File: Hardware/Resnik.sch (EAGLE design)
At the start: 99 parts, among them J2 CONN_82.54_SCREW, J3 CONN_42.54_SCREW, J4 CONN_82.54_SCREW, Q1 DMG3404, Q2 DMG3404, Q3 FDN360P, Q4 FDN360P, U1 TPS61030RSA, U10 MIC2039MT, U11 MIC2039MT, U12 SN74AUP2G08DQE, U13 SN74AUP1G04DCK, U14 MIC2039MT, U15 MIC2039MT, U16 SN74AUP2G08DQE, U17 SN74AUP1G04DCK, U18 TXS0102DQM, U19 LTC4412S6, U2 TPS62822DLC, U3 TLV61220DBV, U4 BQ2980RUG, U6 TPS22917DBV, U7 TPS22917DBV, U8 SN74AUP2G08DQE, U9 SN74AUP2G86SOT833-1

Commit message: Continued schematic additions, prelim part placement
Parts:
- removed R6: 180k, bschulz_passives:R-EU_R0603
- removed R7: 820k, bschulz_passives:R-EU_R0603
- removed U$18: TPS2105, bschulz:TPS2105
- removed U$6: TPS79733, bschulz:TPS79733
- added C22, C24, C28: 0.1uF, bschulz_passives:C-EU0.1UFC0402
- added C23: 10uF, bschulz_passives:C-EU10UFC0805
- added C25: 1uF, bschulz_passives:C-EU0.1UFC0402
- added C26, C27, CX2, CX3: 12pF, bschulz_passives:C-EU12PFC0402
- added C29, C31, C32, C33, C34, C35, C36: 0.1uF, bschulz_passives:C-EUC0402
- added C30: 10uF, bschulz_passives:C-EUC0805
- added D+, D-: 27, bschulz_passives:R-EU_27R0402
- added D2, D3: (no value), bschulz:LM40402.5
- added D4, D5: (no value), bschulz:DIODEDO-214AC
- added F1: PPTC1.5A, bschulz:PPTC1.5A
- added IC1: ATMEGA644M, bschulz:ATMEGA644M
- added ISP2: AVRISP-6, bschulz:AVRISP-6
- added J5, J6, J7: (no value), bschulz:CONN_02SCREW_2.54
- added J8: (no value), bschulz:JST_2MM_MALE
- added JP5, JP6, JP7: JUMPER-SMT_2_NO_SILK, SparkFun-Jumpers:JUMPER-SMT_2_NO_SILK
- added MICRO_USB: MICRO_USB_LONGPADS, bschulz:MICRO_USB_LONGPADS
- added Q5: FDN360P, transistor-power:FDN360P
- added Q6: DMG3404, bschulz:MOSFET-NCH-DMG3404L
- added R35, R36, R37, R38, R39, R40, R41, R42: 330, bschulz_passives:R-EU_330R0402
- added R43, R44: 10k, bschulz_passives:R-EU_10KR0402
- added R45, R48, R49: 10k, bschulz_passives:R-EU_R0402
- added R46: 180k, bschulz_passives:R-EU_R0402
- added R47: 120k, bschulz:R-EU_R0603
- added R50: 330R, bschulz:R-EU_R0603
- added R51: (no value), bschulz:R-EU_R0603
- added R52, R53: 10k, bschulz_passives:R-EU_P10KR0603
- added U$1: CRYSTAL8MHZ5X3.2, bschulz:CRYSTAL8MHZ5X3.2
- added U$13: SN74LVC1G3157DRL, bschulz:SN74LVC1G3157DRL
- added U$15, U$16: CLVBA-FKA, bschulz:CLVBA-FKA
- added U$17: SN74AUP3G34DCU, bschulz:SN74AUP3G34DCU
- added U$2: MICROSD, bschulz:MICROSD
- added U$3: TPL5111DDC, bschulz:TPL5111DDC
- added U$5, U$9: BUTTON4.2X3.2, bschulz:BUTTON4.2X3.2
- added U20, U24: TPS22917DBV, bschulz:TPS22917DBV
- added U21: TXS0102DQM, bschulz:TXS0102DQM
- added U23: FT231X-Q, bschulz:FT231X-Q
- added U25, U26: TXS0108RGY, bschulz:TXS0108RGY
- added U27: TXS0104RGY, bschulz:TXS0104RGY
- added U28: MCP4726A2SOT-23, bschulz:MCP4726A2SOT-23
- added U29, U30: ADS1115, bschulz:ADS1115
- added U31: INA211DCK, bschulz:INA211DCK
- added U32: INA210DCK, bschulz:INA210DCK
- added U33: TCA9555RTW, bschulz:TCA9555RTW
- C1: value 22uF -> 4.7uF
- C10: value 0.1uF -> 22uF; device bschulz_passives:C-EUC0402 -> bschulz_passives:C-EUC0805
- C12: value 22uF -> 0.1uF; device bschulz_passives:C-EUC0805 -> bschulz_passives:C-EUC0402
- C13: value 10uF -> 1uF; device bschulz_passives:C-EUC0805 -> bschulz_passives:C-EUC0603
- C14: value 1uF -> 10uF; device bschulz_passives:C-EUC0603 -> bschulz_passives:C-EUC0805
- C15, C16: value 22uF -> 0.1uF; device bschulz_passives:C-EUC0805 -> bschulz_passives:C-EU0.1UFC0402
- C18: value 0.1uF -> 1uF; device bschulz_passives:C-EU0.1UFC0402 -> bschulz_passives:C-EU1UFC0603
- C19, C20: value 0.1uF -> 22uF; device bschulz_passives:C-EU0.1UFC0402 -> bschulz_passives:C-EUC0805
- C2: value 220uF -> 22uF; device bschulz_passives:CTANT_EU2917 -> bschulz_passives:C-EUC0805
- C21: value 1uF -> 0.1uF; device bschulz_passives:C-EU1UFC0603 -> bschulz_passives:C-EU0.1UFC0402
- C3: value 2.2uF -> 10uF
- C4: value 4.7uF -> 10uF
- C5: value 68pF -> 220uF; device bschulz_passives:C-EUC0402 -> bschulz_passives:CTANT_EU2917
- C6: value 22uF -> 68pF; device bschulz_passives:C-EUC0805 -> bschulz_passives:C-EUC0402
- C7: value 22uF -> 2.2uF
- C8, C9: value 10uF -> 22uF
- J1: value (none) -> CONN_82.54_SCREW; device bschulz:CONN_102.54_SCREW -> bschulz:CONN_82.54_SCREW
- J2: value CONN_82.54_SCREW -> (none); device bschulz:CONN_82.54_SCREW -> bschulz:CONN_102.54_SCREW
- J3: value CONN_42.54_SCREW -> CONN_82.54_SCREW; device bschulz:CONN_42.54_SCREW -> bschulz:CONN_82.54_SCREW
- J4: value CONN_82.54_SCREW -> CONN_42.54_SCREW; device bschulz:CONN_82.54_SCREW -> bschulz:CONN_42.54_SCREW
- L1: value 10uH -> 6.8uH; device bschulz:INDUCTORXHMI_6.65X6.45 -> bschulz:INDUCTOR1008
- L2: value 1uH -> 10uH; device bschulz:INDUCTORLQS_3X3 -> bschulz:INDUCTORXHMI_6.65X6.45
- L3: value 6.8uH -> 1uH; device bschulz:INDUCTOR1008 -> bschulz:INDUCTORLQS_3X3
- R1, R9: value 1.62M -> 180k
- R11: value 20R -> 330R
- R12: value 330R -> 3m; device bschulz:R-EU_R0402 -> bschulz_passives:R-EU_R0805
- R13: value (none) -> 20R
- R14: value 100R -> (none)
- R15: value 2k -> 91k
- R16: value 3m -> 100R; device bschulz_passives:R-EU_R0805 -> bschulz:R-EU_R0402
- R17: value 91k -> 2k
- R2: value 360k -> 1.62M
- R21: value 10k -> (none); device bschulz_passives:R-EU_R0402 -> bschulz:R-EU_R0603
- R22: value 287R -> 10k; device bschulz_passives:R-EU_R0603 -> bschulz_passives:R-EU_10KR0402
- R23, R24, R25: value 287R -> 10k; device bschulz_passives:R-EU_R0603 -> bschulz_passives:R-EU_R0402
- R27, R28, R29, R30: device bschulz_passives:R-EU_R0603 -> bschulz_passives:R-EU_R0402
- R3: value 1.62M -> 360k
- R31, R32: value 10k -> 287R
- R33: value 10k -> 287R; device bschulz_passives:R-EU_10KR0402 -> bschulz_passives:R-EU_R0402
- R34: value (none) -> 287R; device bschulz:R-EU_R0603 -> bschulz_passives:R-EU_R0402
- R4: value 180k -> 1.62M
- R8: value 180k -> 820k
- U1: value TPS61030RSA -> TLV61220DBV; device bschulz:TPS61030RSA -> bschulz:TLV61220DBV
- U10: value MIC2039MT -> SN74AUP1G04DCK; device bschulz:MIC2039MT -> bschulz:SN74AUP1G04DCK
- U11: value MIC2039MT -> SN74AUP2G86SOT833-1; device bschulz:MIC2039MT -> bschulz:SN74AUP2G86SOT833-1
- U13: value SN74AUP1G04DCK -> SN74AUP2G08DQE; device bschulz:SN74AUP1G04DCK -> bschulz:SN74AUP2G08DQE
- U14: value MIC2039MT -> SN74AUP2G08DQE; device bschulz:MIC2039MT -> bschulz:SN74AUP2G08DQE
- U16: value SN74AUP2G08DQE -> MIC2039MT; device bschulz:SN74AUP2G08DQE -> bschulz:MIC2039MT
- U17: value SN74AUP1G04DCK -> MIC2039MT; device bschulz:SN74AUP1G04DCK -> bschulz:MIC2039MT
- U18: value TXS0102DQM -> MIC2039MT; device bschulz:TXS0102DQM -> bschulz:MIC2039MT
- U19: value LTC4412S6 -> TPS22917DBV; device bschulz:LTC4412S6 -> bschulz:TPS22917DBV
- U3: value TLV61220DBV -> TPS61032RSA; device bschulz:TLV61220DBV -> bschulz:TPS61032RSA
- U4: value BQ2980RUG -> (none); device bschulz:BQ2980RUG -> bschulz:LT3652DD
- U5: value (none) -> BQ2980RUG; device bschulz:LT3652DD -> bschulz:BQ2980RUG
- U6: value TPS22917DBV -> TPS2105; device bschulz:TPS22917DBV -> bschulz:TPS2105
- U7: value TPS22917DBV -> LTC4412S6; device bschulz:TPS22917DBV -> bschulz:LTC4412S6
- U8: value SN74AUP2G08DQE -> TPS79733; device bschulz:SN74AUP2G08DQE -> bschulz:TPS79733
- U9: value SN74AUP2G86SOT833-1 -> SN74AUP1G04DCK; device bschulz:SN74AUP2G86SOT833-1 -> bschulz:SN74AUP1G04DCK
- renumbered U$12 to U22
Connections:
- removed net N$1: R3.1, R4.2, U1.FB
- removed net N$17: U6.QOD, U6.VOUT
- removed net N$19: U7.QOD, U7.VOUT
- removed net N$42: R32.2, S2.P
- removed net N$9 (its old number): L3.2, U3.SW
- new net 3V3: C25.1, IC1.AREF, IC1.AVCC, IC1.VCC, IC1.VCC@1, IC1.VCC@2, ISP2.VCC, R44.2, U$16.ANODE
- new net 3V3_AUX_CTRL: IC1.(PCINT22/TOSC1)PC6
- new net 3V3_FTDI: C24.1, U23.3V3OUT, U23.RESET#, U23.VCCIO
- new net ADC_0: JP7.1, U30.AIN0
- new net ADC_1: U30.AIN1
- new net ADC_2: U30.AIN2
- new net ADC_3: JP6.1, U30.AIN3
- new net ADC_EXT: IC1.(PCINT0/ADC0)PA0
- new net ADC_EXT_ALERT: U30.ALERT
- new net ADC_OB_ALERT: U29.ALERT
- new net ALIVE_LED: IC1.(PCINT20/TDO)PC4, R39.2
- new net BAT_SENSE: IC1.(PCINT2/ADC2)PA2
- new net BUS_LOGIC_EN_PRIME: R48.1, U25.EN, U27.EN
- new net BUS_LOGIC_EN_SEC: R49.1, U26.EN
- new net CS_EXT: U27.A4
- new net CS_OUT: U27.B4
- new net DAC_OUT: C31.1, U28.VOUT
- new net DTR: C28.1, U23.DTR#
- new net EN_BUS_SEC: R25.1, U12.A1, U12.B2
- new net FEATHER_BAT: U24.QOD, U24.VOUT
- new net FEATHER_EN: Q5.G, R46.1
- new net GPIO_0: U25.A3
- new net GPIO_0_OUT: U25.B3
- new net GPIO_1: U25.A4
- new net GPIO_1_OUT: U25.B4
- new net GPIO_2: U26.A3
- new net GPIO_2_OUT: U26.B3
- new net GPIO_3: U26.A4
- new net GPIO_3_OUT: U26.B4
- new net GPIO_EXT: IC1.(PCINT11/OC0A/AIN1)PB3
- new net I_LI: U29.AIN2, U31.OUT
- new net I_SOLAR: U29.AIN0, U32.OUT
- new net LED1: IC1.(PCINT29/OC1A)PD5, R42.1
- new net LED2: IC1.(PCINT30/OC2B/ICP)PD6, R40.1
- new net LED3: IC1.(PCINT31/OC2A)PD7, R41.1
- new net LOG_INT: IC1.(PCINT4/ADC4)PA4, R43.1, U$5.3, U$5.4
- new net MISO: IC1.(PCINT14/MISO)PB6, ISP2.MISO, U$2.DATA_OUT, U27.A1
- new net MISO_OUT: U27.B1
- new net MOSI: IC1.(PCINT13/MOSI)PB5, ISP2.MOSI, U$17.2A, U27.A2
- new net MOSI_BUF: U$17.2Y, U$2.DATA_IN
- new net MOSI_OUT: U27.B2
- new net N$44: R38.2, U23.TXD
- new net N$47: R37.2, U23.RXD
- new net N$48: CX3.2, D+.2, MICRO_USB.D+
- new net N$49: CX2.2, D-.2, MICRO_USB.D-
- new net N$5: L2.2, U3.SW
- new net N$50: D+.1, U23.USBDP
- new net N$51: R36.2, U23.CBUS1
- new net N$52: D-.1, U23.USBDM
- new net N$53: R36.1, U$16.RED_CATH
- new net N$54: R35.1, U$16.BLUE_CATH
- new net N$56: R39.1, U$16.GREEN_CATH
- new net N$57: R35.2, U23.CBUS2
- new net N$58: R40.2, U$15.BLUE_CATH
- new net N$59: R41.2, U$15.GREEN_CATH
- new net N$60: R42.2, U$15.RED_CATH
- new net N$61: C27.2, IC1.XTAL2, U$1.2
- new net N$62: C26.2, IC1.XTAL1, U$1.1
- new net N$63: Q5.D, R47.2, U$3.DELAY
- new net N$64: U$3.DRVN, U24.ON
- new net N$65: JP7.2, R53.2
- new net N$66: JP6.2, R52.2
- new net N$67: C10.1, D5.C, U4.VIN, U4.VIN_REG
- new net PG: IC1.(PCINT18/TCK)PC2
- new net RST: C28.2, IC1.RESET, ISP2.RST, R44.1, U$9.3, U$9.4
- new net RX: IC1.(PCINT24/RXD0)PD0, R38.1
- new net RX_EXT: IC1.(PCINT26/INT0)PD2, U25.A6, U26.A6
- new net RX_OUT_PRIME: U25.B6
- new net RX_OUT_SEC: U26.B6
- new net SCK: IC1.(PCINT15/SCK)PB7, ISP2.SCK, U$17.1A, U27.A3
- new net SCK_BUF: U$17.1Y, U$2.SCLK
- new net SCK_OUT: U27.B3
- new net SCL_OUT_PRIME: U25.B2
- new net SCL_OUT_SEC: U26.B2
- new net SDA_CTRL: IC1.(PCINT21/TDI)PC5, U$13.S
- new net SDA_EXT: JP5.2, U$13.B2, U25.A1, U26.A1
- new net SDA_OUT_PRIME: U25.B1
- new net SDA_OUT_SEC: U26.B1
- new net SD_CD: IC1.(PCINT9/CLKO/T1)PB1, R45.1, U$2.CARD_DETECT
- new net SD_CS: IC1.(PCINT12/OC0B/!SS!)PB4, U$17.3A
- new net SD_CS_BUF: U$17.3Y, U$2.CS
- new net SOLAR_SENSE+: L4.2, R20.1, U32.IN+, U4.SENSE
- new net THERM_SENSE: IC1.(PCINT1/ADC1)PA1
- new net TX: IC1.(PCINT25/TXD0)PD1, R37.1
- new net TX_EXT: IC1.(PCINT27/INT1)PD3, U25.A5, U26.A5
- new net TX_OUT_PRIME: U25.B5
- new net TX_OUT_SEC: U26.B5
- new net VBAT_SW_CTRL: IC1.(PCINT19/TMS)PC3
- new net VBUS_SEC: C19.1, U15.VOUT, U16.VOUT, U26.VB
- new net VREF: C32.1, D2.C, IC1.(PCINT3/ADC3)PA3, R50.1, U28.VREF
- new net VSWITCH_CTRL: IC1.(PCINT28/OC1B)PD4
- new net VUSB_POWER: F1.2, Q4.D
- new net V_PRIME-: J5.1, Q6.D
- new net WD_DONE: U$3.DONE
- net 3V3_AUX: now also C21.1, C8.1, C9.1, L3.2, R25.2, R45.2, R48.2, R49.2, R8.2, U$13.VCC, U$17.VCC, U$2.VDD, U10.VCC, U16.VIN, U18.VIN, U21.EN, U21.VA, U25.VA, U26.VA, U27.VA, U9.VCC; no longer C17.1, C5.1, C7.1, L2.2, R21.2, R7.2, U10.VIN, U14.VIN, U16.VCC, U17.VCC, U18.EN, U18.VA
- net 3V3_AUX_PG: now also R1.1; no longer R6.1
- net 3V3_CORE: now also C18.1, Q5.S, R22.2, R43.2, R46.2, U$15.ANODE, U$3.EN, U$3.VDD, U11.VCC, U14.VCC, U8.VOUT; no longer C21.1, R33.2, U$6.VOUT, U8.VCC, U9.VCC
- net 5V_AUX: now also C1.1, C29.1, C30.1, C33.1, C34.1, C35.1, C36.1, C5.+, C7.1, R1.2, R10.2, R50.2, R51.2, U17.VIN, U21.VB, U28.VDD, U29.VDD, U3.VOUT, U30.ADDR, U30.VDD, U31.V+, U32.V+; no longer C2.+, C3.1, C4.1, R3.2, R5.2, R6.2, U1.VOUT, U11.VIN, U18.VB
- net 5V_LP: now also C15.1, C4.1, R4.2, U1.VOUT, U6.EN, U6.IN1; no longer C18.1, C9.1, R9.2, U$18.EN, U$18.IN1, U3.VOUT
- net BMS_CTR: now also R16.1; no longer R14.1
- net C0: now also U11.A1, U11.B2, U14.B1; no longer U8.B1, U9.A1, U9.B2
- net C1: now also U11.A2, U11.B1, U14.B2; no longer U8.B2, U9.A2, U9.B1
- net EN_BUS_PRIME: now also U13.A1, U13.B2; no longer R21.1, U12.A1, U12.B2, U16.A1, U16.B2
- net FAULT_PRIME: now also U16.!FAULT, U17.!FAULT, U18.!FAULT; no longer U10.!FAULT, U11.!FAULT, U14.!FAULT
- net GND: now also C14.2, C2.2, C22.2, C23.2, C24.2, C25.2, C26.1, C27.1, C29.2, C30.2, C31.2, C32.2, C33.2, C34.2, C35.2, C36.2, C5.-, CX2.1, CX3.1, D2.A, D3.A, D4.A, IC1.EXP, IC1.GND, IC1.GND@1, IC1.GND@2, IC1.GND@3, ISP2.GND, J7.1, MICRO_USB.GND, Q6.S, R12.2, R14.1, R23.1, R24.1, R28.2, R29.1, R3.1, R30.2, R47.1, R5.1, R52.1, R53.1, R9.1, U$13.GND, U$17.GND, U$2.CARD_DETECT1, U$2.GND, U$2.GND1, U$2.VSS, U$3.GND, U$5.1, U$5.2, U$9.1, U$9.2, U20.GND, U21.GND, U23.CTS#, U23.GND@13, U23.GND@21, U23.GND@3, U24.GND, U28.VSS, U29.ADDR, U29.GND, U3.PGND, U3.SYNC, U30.GND, U31.GND, U31.IN+, U32.GND, U32.REF, U4.GND_PAD, U4.TIMER, U5.CS; no longer C13.2, C2.-, C6.2, R10.1, R13.1, R16.2, R2.1, R22.1, R24.2, R29.2, R31.1, R32.1, R4.1, R8.1, U$18.GND, U$6.GND, U1.PGND, U1.SYNC, U4.CS, U5.GND_PAD, U5.TIMER
- net LBI: now also R10.1, U3.LBO; no longer R5.1, U1.LBO
- net LI+: now also J6.2, J8.+, R13.2, U29.AIN1; no longer R12.2
- net LI-: now also J6.1, J8.-, R12.1, U31.IN-, U5.VSS; no longer R16.1, U4.VSS
- net MPPT_CHRG: now also U4.!CHRG; no longer U5.!CHRG
- net MPPT_FAULT: now also U4.!FAULT; no longer U5.!FAULT
- net MPPT_SHDN: now also U4.!SHDN; no longer U5.!SHDN
- net N$10: now also U5.DSG; no longer U4.DSG
- net N$11: now also R17.2, U5.PACK; no longer R15.2, U4.PACK
- net N$12: now also R15.1; no longer R17.1
- net N$13: now also C12.1, R16.2, U5.CTR; no longer C10.1, R13.2, U4.CTR
- net N$14: now also R13.1, U5.BAT; no longer R11.1, U4.BAT
- net N$15: now also R15.2, U4.VFB; no longer R17.2, U5.VFB
- net N$16: now also R11.1, U5.VDD; no longer R12.1, U4.VDD
- net N$18: now also C13.2, U4.BOOST; no longer C14.2, U5.BOOST
- net N$2: now also L3.1; no longer L2.1
- net N$20: now also C13.1, D4.C, U4.SW; no longer C14.1, U5.SW
- net N$21: now also D3.C, R51.1, U31.REF; no longer L4.2, R20.1, U5.SENSE
- net N$22: now also U11.Y1, U14.A1; no longer U8.A1, U9.Y1
- net N$23: now also U14.Y1, U19.ON; no longer U7.ON, U8.Y1
- net N$24: now also U14.Y2, U20.ON; no longer U6.ON, U8.Y2
- net N$25: now also U11.Y2, U14.A2; no longer U8.A2, U9.Y2
- net N$26: now also U10.Y, U13.A2; no longer U12.A2, U13.Y
- net N$27: now also R29.2, R33.2, U17.ILIMIT; no longer R22.2, R23.2, U11.ILIMIT
- net N$28: now also R24.2, S2.P, U10.A, U13.B1; no longer R31.2, S1.P, U12.B1, U13.A
- net N$29: now also U13.Y1, U17.EN; no longer U11.EN, U12.Y1
- net N$3: now also C6.2, R8.1, R9.2; no longer C5.2, R7.1, R8.2
- net N$30: now also U13.Y2, U18.EN; no longer U10.EN, U12.Y2
- net N$31: now also JP3.2, R33.1; no longer JP1.2, R23.1
- net N$32: now also JP4.2, R34.2; no longer JP2.2, R25.2
- net N$33: now also R30.1, R34.1, U18.ILIMIT; no longer R24.1, R25.1, U10.ILIMIT
- net N$34: now also U12.A2, U9.Y; no longer U16.A2, U17.Y
- net N$35: now also R23.2, S1.P, U12.B1, U9.A; no longer U16.B1, U17.A
- net N$36: now also U12.Y1; no longer U16.Y1
- net N$37: now also U12.Y2, U16.EN; no longer U14.EN, U16.Y2
- net N$38: now also R31.2; no longer R28.2
- net N$39: now also JP1.2, R31.1; no longer JP3.2, R28.1
- net N$4: now also R2.1, R3.2, U3.LBI; no longer R1.1, R2.2, U1.LBI
- net N$40: now also JP2.2, R32.2; no longer JP4.2, R30.2
- net N$41: now also R28.1, R32.1, U16.ILIMIT; no longer R29.1, R30.1, U14.ILIMIT
- net N$45: now also Q4.G, U7.GATE; no longer Q3.G, U19.GATE
- net N$46: now also Q3.G, R21.1, U7.STAT; no longer Q4.G, R34.1, U19.STAT
- net N$7: now also R4.1, R5.2, U1.FB; no longer R10.2, R9.1, U3.FB
- net N$8: now also U5.CHG; no longer U4.CHG
- net PG_LDO: now also R22.1, U8.PG; no longer R33.1, U$6.PG
- net RTC_INT: now also IC1.(PCINT10/INT2/AIN0)PB2
- net SCL: now also IC1.(PCINT16/SCL)PC0, U21.A2, U25.A2, U26.A2; no longer U18.A2
- net SCL_5V: now also U21.B2, U28.SCL, U29.SCL, U30.SCL; no longer U18.B2
- net SDA: now also IC1.(PCINT17/SDA)PC1, U$13.A, U21.A1; no longer U18.A1
- net SDA_5V: now also U21.B1, U28.SDA, U29.SDA, U30.SDA; no longer U18.B1
- net SDA_OB: now also JP5.1, U$13.B1
- net VBAT+: now also C17.1, U6.OUT, U8.VIN; no longer C20.1, U$18.OUT, U$6.VIN
- net VBUS_PRIME: now also C20.1, U17.VOUT, U18.VOUT, U25.VB, U27.VB; no longer C15.1, C16.1, U10.VOUT, U11.VOUT, U14.VOUT, U15.VOUT
- net VUSB: now also C22.1, C23.1, F1.1, MICRO_USB.VDD, U23.VCC; no longer Q3.D
- net V_BETA: now also C3.1, L1.1, R21.2, U1.EN, U1.VBAT, U20.VIN, U7.SENSE; no longer C8.1, L3.1, R34.2, U19.SENSE, U3.EN, U3.VBAT, U6.VIN
- net V_BETA_CTL: now also U7.CTL; no longer U19.CTL
- net V_HP: now also C2.1, L2.1, R2.2, U19.QOD, U19.VOUT, U20.QOD, U20.VOUT, U3.EN, U3.VBAT; no longer C1.1, L1.1, R1.2, U1.EN, U1.VBAT
- net V_LI: now also C14.1, Q3.D, R17.1, U24.VIN, U32.IN-, U4.BAT, U7.VIN; no longer C13.1, Q4.D, R15.1, U19.VIN, U5.BAT
- net V_PRIME: now also C16.1, J5.2, Q6.G, U19.VIN, U29.AIN3, U6.IN2; no longer C19.1, U$18.IN2, U7.VIN
- net V_SOLAR: now also D5.A, J7.2; no longer C12.1, U5.VIN, U5.VIN_REG
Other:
- note added: "ADR = 0x49"
- note added: "Also ext PWM"
- note added: "Ext Int0"
- note added: "Ext Int1"
- note added: "ICSP"
- note added: "Indicators"
- note added: "Jump SDA channels together, prevents using occupied addresses on the external I2C port"
- note added: "Pin 0"
- note added: "Pin 1"
- note added: "Pin 10"
- note added: "Pin 11"
- note added: "Pin 12"
- note added: "Pin 13"
- note added: "Pin 14"
- note added: "Pin 15"
- note added: "Pin 16"
- note added: "Pin 17"
- note added: "Pin 18"
- note added: "Pin 19"
- note added: "Pin 2"
- note added: "Pin 20"
- note added: "Pin 21"
- note added: "Pin 22"
- note added: "Pin 23"
- note added: "Pin 3"
- note added: "Pin 4"
- note added: "Pin 5"
- note added: "Pin 6"
- note added: "Pin 7"
- note added: "Pin 8"
- note added: "Pin 9"
- note added: "Pin A0"
- note added: "Pin A1"
- note added: "Pin A2"
- note added: "Pin A3"
- note added: "Pin A4"
- note added: "Pin A5"
- note added: "Pin A6"
- note added: "Pin A7"
- note added: "Reverse Polarity Protection"
- note added: "USB & ISP"

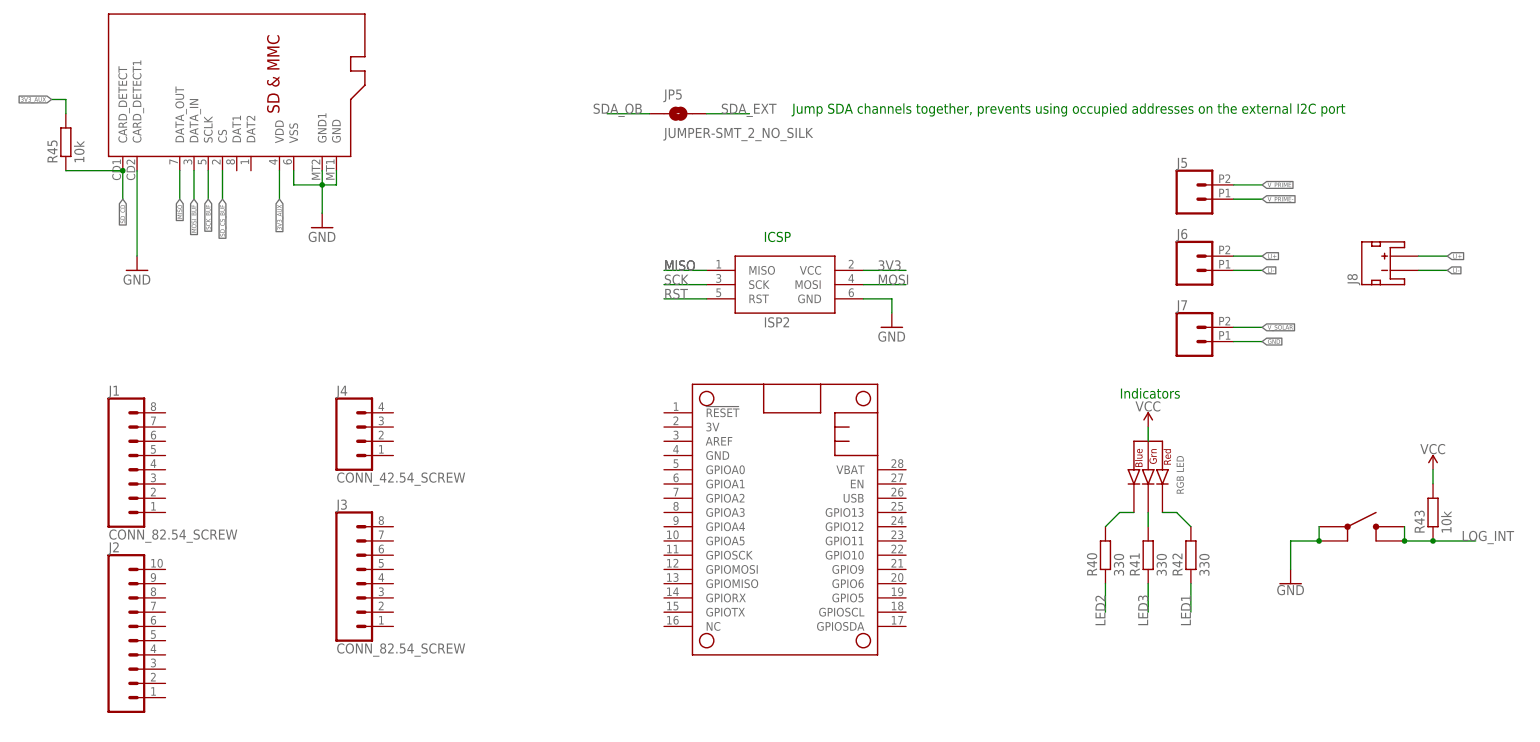
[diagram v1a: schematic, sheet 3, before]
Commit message: Preliminary power section layout
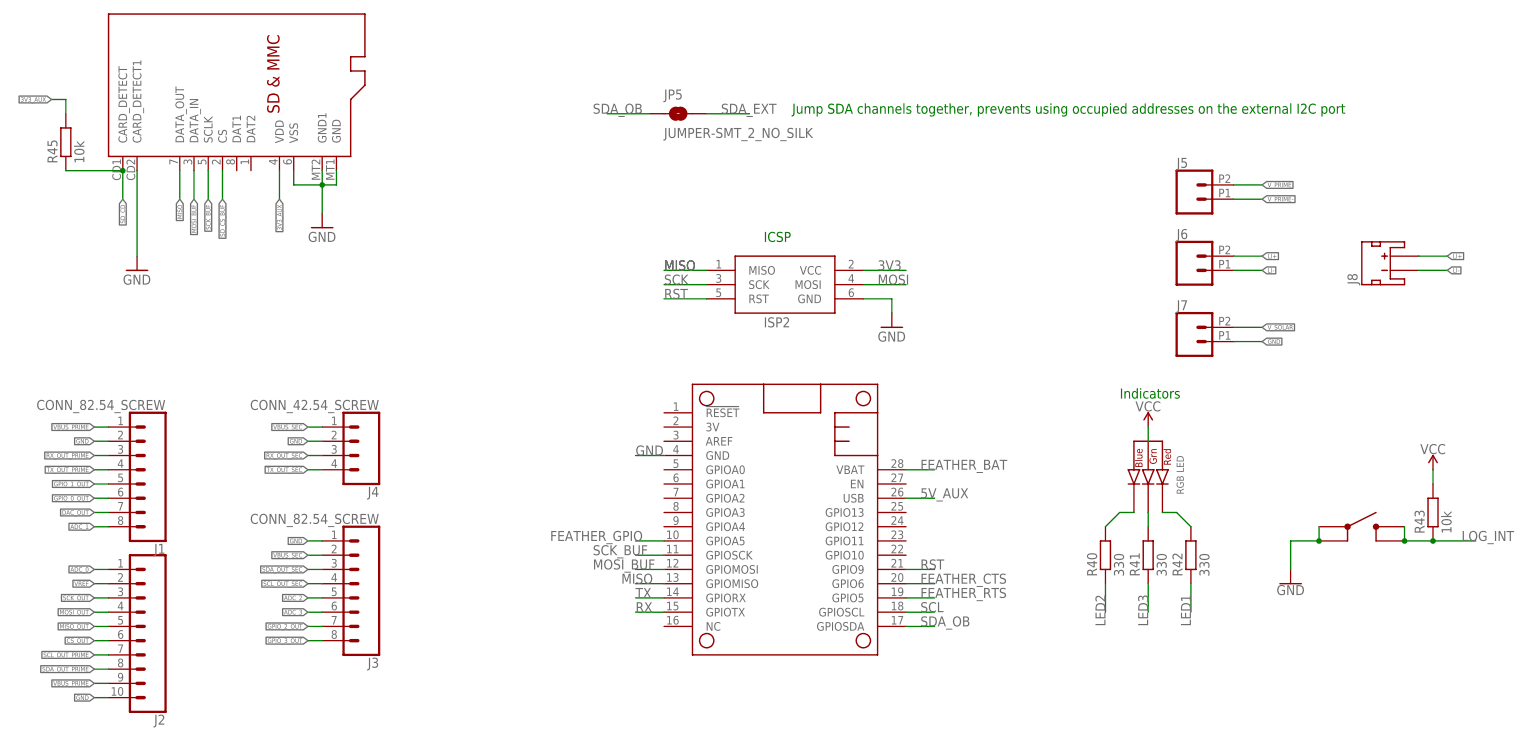
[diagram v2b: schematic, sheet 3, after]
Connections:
- removed net 3V3_AUX_CTRL: IC1.(PCINT22/TOSC1)PC6
- removed net ADC_EXT: IC1.(PCINT0/ADC0)PA0
- removed net BAT_SENSE: IC1.(PCINT2/ADC2)PA2
- removed net GPIO_EXT: IC1.(PCINT11/OC0A/AIN1)PB3
- removed net PG: IC1.(PCINT18/TCK)PC2
- removed net THERM_SENSE: IC1.(PCINT1/ADC1)PA1
- removed net VBAT_SW_CTRL: IC1.(PCINT19/TMS)PC3
- removed net VSWITCH_CTRL: IC1.(PCINT28/OC1B)PD4
- new net FEATHER_CTS: IC1.(PCINT6/ADC6)PA6, MS1.GPIO6
- new net FEATHER_GPIO: IC1.(PCINT5/ADC5)PA5, MS1.GPIOA5
- new net FEATHER_RTS: IC1.(PCINT7/ADC7)PA7, MS1.GPIO5
- new net GLOBAL_INT: IC1.(PCINT3/ADC3)PA3, U33.!INT
- net 3V3_CORE: now also U33.VCC
- net 5V_AUX: now also MS1.USB
- net ADC_0: now also J2.1
- net ADC_1: now also J1.8
- net ADC_2: now also J3.5
- net ADC_3: now also J3.6
- net C0: now also IC1.(PCINT18/TCK)PC2
- net C1: now also IC1.(PCINT19/TMS)PC3
- net CS_OUT: now also J2.6
- net DAC_OUT: now also J1.7
- net EN_BUS_PRIME: now also IC1.(PCINT22/TOSC1)PC6
- net EN_BUS_SEC: now also IC1.(PCINT23/TOSC2)PC7
- net FEATHER_BAT: now also MS1.VBAT
- net GND: now also J1.2, J2.10, J3.1, J4.2, MS1.GND, U33.A0, U33.A1, U33.A2, U33.GND
- net GPIO_0: now also IC1.(PCINT28/OC1B)PD4
- net GPIO_0_OUT: now also J1.6
- net GPIO_1_OUT: now also J1.5
- net GPIO_2: now also IC1.(PCINT11/OC0A/AIN1)PB3, U26.A4; no longer U26.A3
- net GPIO_2_OUT: now also J3.7, U26.B4; no longer U26.B3
- net GPIO_3: now also U26.A3; no longer U26.A4
- net GPIO_3_OUT: now also J3.8, U26.B3; no longer U26.B4
- net MISO: now also MS1.GPIOMISO
- net MISO_OUT: now also J2.5
- net MOSI_BUF: now also MS1.GPIOMOSI
- net MOSI_OUT: now also J2.4
- net RST: now also MS1.GPIO9
- net RX: now also MS1.GPIOTX
- net RX_EXT: now also U26.A1; no longer U26.A6
- net RX_OUT_PRIME: now also J1.3
- net RX_OUT_SEC: now also J4.3, U26.B1; no longer U26.B6
- net SCK_BUF: now also MS1.GPIOSCK
- net SCK_OUT: now also J2.3
- net SCL: now also MS1.GPIOSCL, U26.A5, U33.SCL; no longer U26.A2
- net SCL_OUT_PRIME: now also J2.7
- net SCL_OUT_SEC: now also J3.4, U26.B5; no longer U26.B2
- net SDA_EXT: now also U26.A6; no longer U26.A1
- net SDA_OB: now also MS1.GPIOSDA, U33.SDA
- net SDA_OUT_PRIME: now also J2.8
- net SDA_OUT_SEC: now also J3.3, U26.B6; no longer U26.B1
- net TX: now also MS1.GPIORX
- net TX_EXT: now also U26.A2; no longer U26.A5
- net TX_OUT_PRIME: now also J1.4
- net TX_OUT_SEC: now also J4.4, U26.B2; no longer U26.B5
- net VBUS_PRIME: now also J1.1, J2.9
- net VBUS_SEC: now also J3.2, J4.1
- net VREF: now also J2.2; no longer IC1.(PCINT3/ADC3)PA3
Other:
- note added: "ADD: MPPT, CHRG (Input) MPPT, FAULT (Input) MPPT, SHDN (Output) Feather PowerOn (Output) ADC, OnBoard, Alert/RDY (Input, Interrupt) ADC, OffBoard, Alert/RDY (Input, Interrupt) Vusb (Input) LevelShifter, Primary Bus, EN (Output) LevelShifter, Secondary Bus, EN (Output) BMS, CTR (Output) BusPowerSwitch, Primary Bus, Fault (Input) BusPowerSwitch, Secondary Bus, Fault (Input) HighPowerBoost, LBO (Inp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"
- note added: "Add: GPIO1 GPIO3"
- moved on the sheet: J1, J2, J3, J4

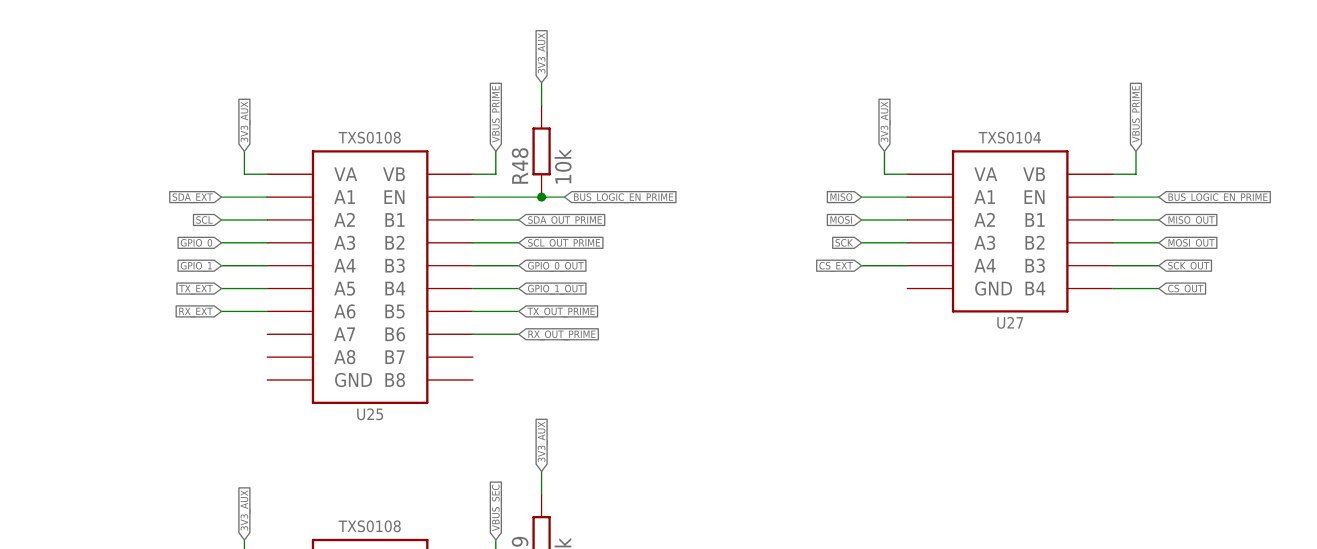
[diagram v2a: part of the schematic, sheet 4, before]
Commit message: Continued layout, board size change
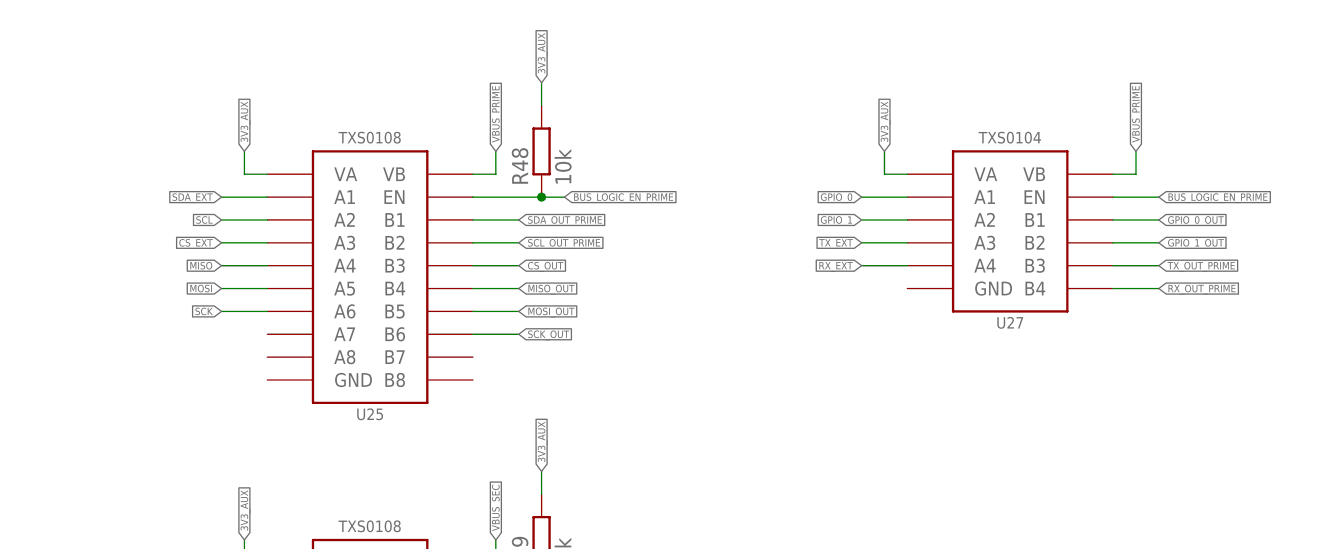
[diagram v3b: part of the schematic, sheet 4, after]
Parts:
- U10, U9: value SN74AUP1G04DCK -> SN74AUP1G04YFP; device bschulz:SN74AUP1G04DCK -> bschulz:SN74AUP1G04YFP
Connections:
- net CS_EXT: now also U25.A3; no longer U27.A4
- net CS_OUT: now also U25.B3; no longer U27.B4
- net GPIO_0: now also U27.A1; no longer U25.A3
- net GPIO_0_OUT: now also U27.B1; no longer U25.B3
- net GPIO_1: now also U27.A2; no longer U25.A4
- net GPIO_1_OUT: now also U27.B2; no longer U25.B4
- net MISO: now also U25.A4; no longer U27.A1
- net MISO_OUT: now also U25.B4; no longer U27.B1
- net MOSI: now also U25.A5; no longer U27.A2
- net MOSI_OUT: now also U25.B5; no longer U27.B2
- net RX_EXT: now also U27.A4; no longer U25.A6
- net RX_OUT_PRIME: now also U27.B4; no longer U25.B6
- net SCK: now also U25.A6; no longer U27.A3
- net SCK_OUT: now also U25.B6; no longer U27.B3
- net TX_EXT: now also U27.A3; no longer U25.A5
- net TX_OUT_PRIME: now also U27.B3; no longer U25.B5
